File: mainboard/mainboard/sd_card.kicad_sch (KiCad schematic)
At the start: 8 parts

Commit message: Fixing labels
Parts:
- C59: renamed from C?; value (none) -> 100n
- R20, R21, R22, R23, R24, R25: renamed from R?; value (none) -> 10k
- gave numbers to parts that had none: 1
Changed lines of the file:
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@@
   (symbol (lib_id "Device:R") (at 97.79 72.39 0) (unit 1)
     (in_bom yes) (on_board yes) (fields_autoplaced)
-    (property "Reference" "R?" (id 0) (at 100.33 71.1199 0)
+    (property "Reference" "R22" (id 0) (at 100.33 71.1199 0)
       (effects (font (size 1.27 1.27)) (justify left))
     )
-    (property "Value" "" (id 1) (at 100.33 73.6599 0)
+    (property "Value" "10k" (id 1) (at 100.33 73.6599 0)
       (effects (font (size 1.27 1.27)) (justify left))
     )
@@
   (symbol (lib_id "Device:R") (at 106.68 72.39 0) (unit 1)
     (in_bom yes) (on_board yes) (fields_autoplaced)
-    (property "Reference" "R?" (id 0) (at 109.22 71.1199 0)
+    (property "Reference" "R23" (id 0) (at 109.22 71.1199 0)
       (effects (font (size 1.27 1.27)) (justify left))
     )
-    (property "Value" "" (id 1) (at 109.22 73.6599 0)
+    (property "Value" "10k" (id 1) (at 109.22 73.6599 0)
       (effects (font (size 1.27 1.27)) (justify left))
     )
@@
   (symbol (lib_id "power:GND") (at 189.23 115.57 0) (unit 1)
     (in_bom yes) (on_board yes) (fields_autoplaced)
-    (property "Reference" "#PWR?" (id 0) (at 189.23 121.92 0)
+    (property "Reference" "#PWR0159" (id 0) (at 189.23 121.92 0)
       (effects (font (size 1.27 1.27)) hide)
     )
-    (property "Value" "" (id 1) (at 189.23 120.65 0))
+    (property "Value" "GND" (id 1) (at 189.23 120.65 0))
     (property "Footprint" "" (id 2) (at 189.23 115.57 0)
       (effects (font (size 1.27 1.27)) hide)
@@
   (symbol (lib_id "power:+3V3") (at 137.16 62.23 0) (unit 1)
     (in_bom yes) (on_board yes) (fields_autoplaced)
-    (property "Reference" "#PWR?" (id 0) (at 137.16 66.04 0)
+    (property "Reference" "#PWR0157" (id 0) (at 137.16 66.04 0)
       (effects (font (size 1.27 1.27)) hide)
     )
-    (property "Value" "" (id 1) (at 137.16 57.15 0))
+    (property "Value" "+3V3" (id 1) (at 137.16 57.15 0))
     (property "Footprint" "" (id 2) (at 137.16 62.23 0)
       (effects (font (size 1.27 1.27)) hide)
@@
   (symbol (lib_id "Device:C") (at 137.16 71.12 0) (unit 1)
     (in_bom yes) (on_board yes) (fields_autoplaced)
-    (property "Reference" "C?" (id 0) (at 140.97 69.8499 0)
+    (property "Reference" "C59" (id 0) (at 140.97 69.8499 0)
       (effects (font (size 1.27 1.27)) (justify left))
     )
-    (property "Value" "" (id 1) (at 140.97 72.3899 0)
+    (property "Value" "100n" (id 1) (at 140.97 72.3899 0)
       (effects (font (size 1.27 1.27)) (justify left))
     )
@@
   (symbol (lib_id "Device:R") (at 115.57 72.39 0) (unit 1)
     (in_bom yes) (on_board yes) (fields_autoplaced)
-    (property "Reference" "R?" (id 0) (at 118.11 71.1199 0)
+    (property "Reference" "R24" (id 0) (at 118.11 71.1199 0)
       (effects (font (size 1.27 1.27)) (justify left))
     )
-    (property "Value" "" (id 1) (at 118.11 73.6599 0)
+    (property "Value" "10k" (id 1) (at 118.11 73.6599 0)
       (effects (font (size 1.27 1.27)) (justify left))
     )
@@
   (symbol (lib_id "power:GND") (at 132.08 118.11 0) (unit 1)
     (in_bom yes) (on_board yes) (fields_autoplaced)
-    (property "Reference" "#PWR?" (id 0) (at 132.08 124.46 0)
+    (property "Reference" "#PWR0156" (id 0) (at 132.08 124.46 0)
       (effects (font (size 1.27 1.27)) hide)
     )
-    (property "Value" "" (id 1) (at 132.08 123.19 0))
+    (property "Value" "GND" (id 1) (at 132.08 123.19 0))
     (property "Footprint" "" (id 2) (at 132.08 118.11 0)
       (effects (font (size 1.27 1.27)) hide)
@@
   (symbol (lib_id "Connector:Micro_SD_Card") (at 166.37 95.25 0) (unit 1)
     (in_bom yes) (on_board yes) (fields_autoplaced)
-    (property "Reference" "J?" (id 0) (at 167.005 76.2 0))
+    (property "Reference" "J15" (id 0) (at 167.005 76.2 0))
     (property "Value" "Micro_SD_Card" (id 1) (at 167.005 78.74 0))
     (property "Footprint" "Connector_Card:microSD_HC_Wuerth_693072010801" (id 2) (at 195.58 87.63 0)
@@
   (symbol (lib_id "Device:R") (at 80.01 72.39 0) (unit 1)
     (in_bom yes) (on_board yes) (fields_autoplaced)
-    (property "Reference" "R?" (id 0) (at 82.55 71.1199 0)
+    (property "Reference" "R20" (id 0) (at 82.55 71.1199 0)
       (effects (font (size 1.27 1.27)) (justify left))
     )
-    (property "Value" "" (id 1) (at 82.55 73.6599 0)
+    (property "Value" "10k" (id 1) (at 82.55 73.6599 0)
       (effects (font (size 1.27 1.27)) (justify left))
     )
@@
   (symbol (lib_id "Device:R") (at 124.46 72.39 0) (unit 1)
     (in_bom yes) (on_board yes) (fields_autoplaced)
-    (property "Reference" "R?" (id 0) (at 127 71.1199 0)
+    (property "Reference" "R25" (id 0) (at 127 71.1199 0)
       (effects (font (size 1.27 1.27)) (justify left))
     )
-    (property "Value" "" (id 1) (at 127 73.6599 0)
+    (property "Value" "10k" (id 1) (at 127 73.6599 0)
       (effects (font (size 1.27 1.27)) (justify left))
     )
@@
   (symbol (lib_id "power:GND") (at 137.16 77.47 0) (unit 1)
     (in_bom yes) (on_board yes) (fields_autoplaced)
-    (property "Reference" "#PWR?" (id 0) (at 137.16 83.82 0)
+    (property "Reference" "#PWR0158" (id 0) (at 137.16 83.82 0)
       (effects (font (size 1.27 1.27)) hide)
     )
-    (property "Value" "" (id 1) (at 137.16 82.55 0))
+    (property "Value" "GND" (id 1) (at 137.16 82.55 0))
     (property "Footprint" "" (id 2) (at 137.16 77.47 0)
       (effects (font (size 1.27 1.27)) hide)
@@
   (symbol (lib_id "Device:R") (at 88.9 72.39 0) (unit 1)
     (in_bom yes) (on_board yes) (fields_autoplaced)
-    (property "Reference" "R?" (id 0) (at 91.44 71.1199 0)
+    (property "Reference" "R21" (id 0) (at 91.44 71.1199 0)
       (effects (font (size 1.27 1.27)) (justify left))
     )
-    (property "Value" "" (id 1) (at 91.44 73.6599 0)
+    (property "Value" "10k" (id 1) (at 91.44 73.6599 0)
       (effects (font (size 1.27 1.27)) (justify left))
     )

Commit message: fixed warnings and errors
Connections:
- net SDIO_CLK renamed SDIO.CLK
- net SDIO_CMD renamed SDIO.CMD
- net SDIO_D_0 renamed SDIO.D0
- net SDIO_D_1 renamed SDIO.D1
- net SDIO_D_2 renamed SDIO.D2
- net SDIO_D_3 renamed SDIO.D3
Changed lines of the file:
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@@
     (stroke (width 0) (type default) (color 0 0 0 0))
   )
-  (label "SDIO_CMD" (at 62.23 92.71 180)
+  (label "SDIO.CMD" (at 62.23 92.71 180)
     (effects (font (size 1.27 1.27)) (justify right bottom))
   )
-  (label "SDIO_CLK" (at 62.23 97.79 180)
+  (label "SDIO.CLK" (at 62.23 97.79 180)
     (effects (font (size 1.27 1.27)) (justify right bottom))
   )
-  (label "SDIO_D_0" (at 62.23 102.87 180)
+  (label "SDIO.D0" (at 62.23 102.87 180)
     (effects (font (size 1.27 1.27)) (justify right bottom))
   )
-  (label "SDIO_D_3" (at 62.23 90.17 180)
+  (label "SDIO.D3" (at 62.23 90.17 180)
     (effects (font (size 1.27 1.27)) (justify right bottom))
   )
-  (label "SDIO_D_1" (at 62.23 105.41 180)
+  (label "SDIO.D1" (at 62.23 105.41 180)
     (effects (font (size 1.27 1.27)) (justify right bottom))
   )
-  (label "SDIO_D_2" (at 62.23 87.63 180)
+  (label "SDIO.D2" (at 62.23 87.63 180)
     (effects (font (size 1.27 1.27)) (justify right bottom))
   )
-  (hierarchical_label "SDIO" (shape bidirectional) (at 39.37 85.09 180)
+  (hierarchical_label "SDIO{CMD CLK D[0..3]}" (shape bidirectional) (at 39.37 85.09 180)
     (effects (font (size 1.27 1.27)) (justify right))
   )

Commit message: board almost ready, paths must be aligned
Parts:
- removed R20, R21, R22, R23, R24, R25: 10k, symbol Device:R
- added R801, R802: 10k, Resistor_SMD:R_0603_1608Metric_Pad0.98x0.95mm_HandSolder, symbol Device:R
- C801: renamed from C59; value 100n -> 10u; footprint (none) -> Capacitor_SMD:C_0603_1608Metric_Pad1.08x0.95mm_HandSolder
- renumbered J15 to J801
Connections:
- net +3V3: now also R801.1, R802.1
- net SDIO.D1: now also R802.2
- net SDIO.D2: now also R801.2
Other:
- moved on the sheet: C801

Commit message: motherboard designed
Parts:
- U: renamed from R801; value 10k -> (none); footprint Resistor_SMD:R_0603_1608Metric_Pad0.98x0.95mm_HandSolder -> (none)
- U: renamed from R802; value 10k -> (none); footprint Resistor_SMD:R_0603_1608Metric_Pad0.98x0.95mm_HandSolder -> (none)
- U: renamed from C801; value 10u -> (none); footprint Capacitor_SMD:C_0603_1608Metric_Pad1.08x0.95mm_HandSolder -> (none)
- U: renamed from J801; value Micro_SD_Card -> (none); footprint Connector_Card:microSD_HC_Wuerth_693072010801 -> (none)
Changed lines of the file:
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@@
-(kicad_sch (version 20220104) (generator eeschema)
+(kicad_sch (version 20220404) (generator eeschema)
   (paper "A4")
   (junction (at 113.03 87.63) (diameter 0) (color 0 0 0 0)
@@
   (symbol (lib_id "power:GND") (at 189.23 115.57 0) (unit 1)
     (in_bom yes) (on_board yes) (fields_autoplaced)
-    (property "Reference" "#PWR0804" (id 0) (at 189.23 121.92 0)
-      (effects (font (size 1.27 1.27)) hide)
-    )
-    (property "Value" "GND" (id 1) (at 189.23 120.65 0)
+    (default_instance (reference "U") (unit 1) (value "") (footprint ""))
+    (property "Reference" "U" (id 0) (at 189.23 121.92 0)
+      (effects (font (size 1.27 1.27)) hide)
+    )
+    (property "Value" "" (id 1) (at 189.23 120.65 0)
       (effects (font (size 1.27 1.27)))
     )
@@
   (symbol (lib_id "power:+3V3") (at 162.56 45.72 0) (unit 1)
     (in_bom yes) (on_board yes) (fields_autoplaced)
-    (property "Reference" "#PWR0802" (id 0) (at 162.56 49.53 0)
-      (effects (font (size 1.27 1.27)) hide)
-    )
-    (property "Value" "+3V3" (id 1) (at 162.56 40.64 0)
+    (default_instance (reference "U") (unit 1) (value "") (footprint ""))
+    (property "Reference" "U" (id 0) (at 162.56 49.53 0)
+      (effects (font (size 1.27 1.27)) hide)
+    )
+    (property "Value" "" (id 1) (at 162.56 40.64 0)
       (effects (font (size 1.27 1.27)))
     )
@@
   (symbol (lib_id "Device:R") (at 113.03 72.39 0) (unit 1)
     (in_bom yes) (on_board yes) (fields_autoplaced)
-    (property "Reference" "R801" (id 0) (at 115.57 71.755 0)
-      (effects (font (size 1.27 1.27)) (justify left))
-    )
-    (property "Value" "10k" (id 1) (at 115.57 73.025 0)
-      (effects (font (size 1.27 1.27)) (justify left))
-    )
-    (property "Footprint" "Resistor_SMD:R_0603_1608Metric_Pad0.98x0.95mm_HandSolder" (id 2) (at 111.252 72.39 90)
+    (default_instance (reference "U") (unit 1) (value "") (footprint ""))
+    (property "Reference" "U" (id 0) (at 115.57 71.755 0)
+      (effects (font (size 1.27 1.27)) (justify left))
+    )
+    (property "Value" "" (id 1) (at 115.57 73.025 0)
+      (effects (font (size 1.27 1.27)) (justify left))
+    )
+    (property "Footprint" "" (id 2) (at 111.252 72.39 90)
       (effects (font (size 1.27 1.27)) hide)
     )
@@
   (symbol (lib_id "Device:R") (at 121.92 72.39 0) (unit 1)
     (in_bom yes) (on_board yes) (fields_autoplaced)
-    (property "Reference" "R802" (id 0) (at 124.46 71.755 0)
-      (effects (font (size 1.27 1.27)) (justify left))
-    )
-    (property "Value" "10k" (id 1) (at 124.46 73.025 0)
-      (effects (font (size 1.27 1.27)) (justify left))
-    )
-    (property "Footprint" "Resistor_SMD:R_0603_1608Metric_Pad0.98x0.95mm_HandSolder" (id 2) (at 120.142 72.39 90)
+    (default_instance (reference "U") (unit 1) (value "") (footprint ""))
+    (property "Reference" "U" (id 0) (at 124.46 71.755 0)
+      (effects (font (size 1.27 1.27)) (justify left))
+    )
+    (property "Value" "" (id 1) (at 124.46 73.025 0)
+      (effects (font (size 1.27 1.27)) (justify left))
+    )
+    (property "Footprint" "" (id 2) (at 120.142 72.39 90)
       (effects (font (size 1.27 1.27)) hide)
     )
@@
   (symbol (lib_id "Device:C") (at 162.56 54.61 0) (unit 1)
     (in_bom yes) (on_board yes) (fields_autoplaced)
-    (property "Reference" "C801" (id 0) (at 166.37 53.3399 0)
-      (effects (font (size 1.27 1.27)) (justify left))
-    )
-    (property "Value" "10u" (id 1) (at 166.37 55.8799 0)
-      (effects (font (size 1.27 1.27)) (justify left))
-    )
-    (property "Footprint" "Capacitor_SMD:C_0603_1608Metric_Pad1.08x0.95mm_HandSolder" (id 2) (at 163.5252 58.42 0)
+    (default_instance (reference "U") (unit 1) (value "") (footprint ""))
+    (property "Reference" "U" (id 0) (at 166.37 53.3399 0)
+      (effects (font (size 1.27 1.27)) (justify left))
+    )
+    (property "Value" "" (id 1) (at 166.37 55.8799 0)
+      (effects (font (size 1.27 1.27)) (justify left))
+    )
+    (property "Footprint" "" (id 2) (at 163.5252 58.42 0)
       (effects (font (size 1.27 1.27)) hide)
     )
@@
   (symbol (lib_id "power:GND") (at 132.08 118.11 0) (unit 1)
     (in_bom yes) (on_board yes) (fields_autoplaced)
-    (property "Reference" "#PWR0801" (id 0) (at 132.08 124.46 0)
-      (effects (font (size 1.27 1.27)) hide)
-    )
-    (property "Value" "GND" (id 1) (at 132.08 123.19 0)
+    (default_instance (reference "U") (unit 1) (value "") (footprint ""))
+    (property "Reference" "U" (id 0) (at 132.08 124.46 0)
+      (effects (font (size 1.27 1.27)) hide)
+    )
+    (property "Value" "" (id 1) (at 132.08 123.19 0)
       (effects (font (size 1.27 1.27)))
     )
@@
   (symbol (lib_id "Connector:Micro_SD_Card") (at 166.37 95.25 0) (unit 1)
     (in_bom yes) (on_board yes) (fields_autoplaced)
-    (property "Reference" "J801" (id 0) (at 167.005 76.2 0)
-      (effects (font (size 1.27 1.27)))
-    )
-    (property "Value" "Micro_SD_Card" (id 1) (at 167.005 78.74 0)
-      (effects (font (size 1.27 1.27)))
-    )
-    (property "Footprint" "Connector_Card:microSD_HC_Wuerth_693072010801" (id 2) (at 195.58 87.63 0)
+    (default_instance (reference "U") (unit 1) (value "") (footprint ""))
+    (property "Reference" "U" (id 0) (at 167.005 76.2 0)
+      (effects (font (size 1.27 1.27)))
+    )
+    (property "Value" "" (id 1) (at 167.005 78.74 0)
+      (effects (font (size 1.27 1.27)))
+    )
+    (property "Footprint" "" (id 2) (at 195.58 87.63 0)
       (effects (font (size 1.27 1.27)) hide)
     )
@@
   (symbol (lib_id "power:GND") (at 162.56 60.96 0) (unit 1)
     (in_bom yes) (on_board yes) (fields_autoplaced)
-    (property "Reference" "#PWR0803" (id 0) (at 162.56 67.31 0)
-      (effects (font (size 1.27 1.27)) hide)
-    )
-    (property "Value" "GND" (id 1) (at 162.56 66.04 0)
-      (effects (font (size 1.27 1.27)))
-    )
+    (default_instance (reference "U") (unit 1) (value "") (footprint ""))
+    (property "Reference" "U" (id 0) (at 162.56 67.31 0)
+      (effects (font (size 1.27 1.27)) hide)
+    )
+    (property "Value" "" (id 1) (at 162.56 66.04 0)
+      (effects (font (size 1.27 1.27)))
+    )

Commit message: schematic for gpu extension
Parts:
- C801: renamed from U; value (none) -> 10u; footprint (none) -> Capacitor_SMD:C_0603_1608Metric_Pad1.08x0.95mm_HandSolder
- J801: renamed from U; value (none) -> Micro_SD_Card; footprint (none) -> Connector_Card:microSD_HC_Wuerth_693072010801
- R801, R802: renamed from U; value (none) -> 10k; footprint (none) -> Resistor_SMD:R_0603_1608Metric_Pad0.98x0.95mm_HandSolder

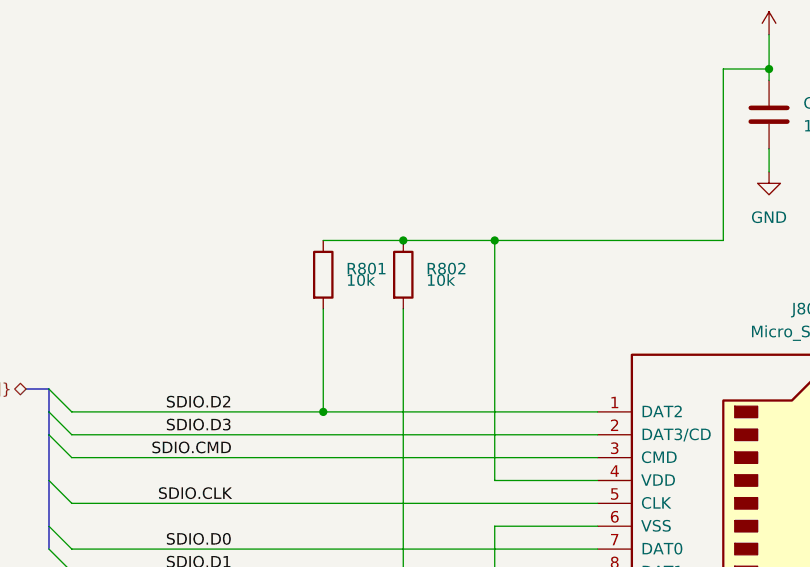
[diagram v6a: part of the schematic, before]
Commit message: gpu and motherboard passes tests, now time for fpga
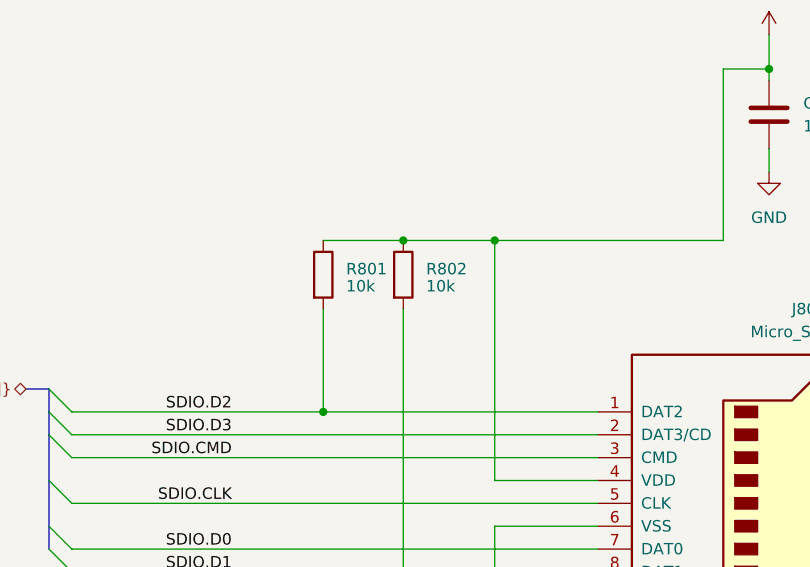
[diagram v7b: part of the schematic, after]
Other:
- title: (none) -> MSPC
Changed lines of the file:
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@@
 (kicad_sch (version 20221004) (generator eeschema)
   (paper "A4")
+  (title_block
+    (title "MSPC")
+    (rev "1")
+  )
   (junction (at 113.03 87.63) (diameter 0) (color 0 0 0 0)
   )
@@
   )
   (symbol (lib_id "Device:R") (at 113.03 72.39 0) (unit 1)
-    (in_bom yes) (on_board yes) (dnp no) (fields_autoplaced)
+    (in_bom yes) (on_board yes) (dnp no)
     (property "Reference" "R801" (at 115.57 71.755 0)
       (effects (font (size 1.27 1.27)) (justify left))
     )
-    (property "Value" "10k" (at 115.57 73.025 0)
+    (property "Value" "10k" (at 115.57 73.66 0)
       (effects (font (size 1.27 1.27)) (justify left))
     )
@@
   )
   (symbol (lib_id "Device:R") (at 121.92 72.39 0) (unit 1)
-    (in_bom yes) (on_board yes) (dnp no) (fields_autoplaced)
+    (in_bom yes) (on_board yes) (dnp no)
     (property "Reference" "R802" (at 124.46 71.755 0)
       (effects (font (size 1.27 1.27)) (justify left))
     )
-    (property "Value" "10k" (at 124.46 73.025 0)
-      (effects (font (size 1.27 1.27)) (justify left))
-    )
+    (property "Value" "10k" (at 124.46 73.66 0)
+      (effects (font (size 1.27 1.27)) (justify left))
+    )

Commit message: refactored mainboard schematic
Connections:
- net +3V3 renamed +3V3_SOUTH
